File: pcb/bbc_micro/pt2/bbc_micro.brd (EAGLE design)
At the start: 56 x 65 mm, 51 parts, among them IC1 STM32F072C8T6, SW1 324_SW, SW2 324_SW, SW3 324_SW

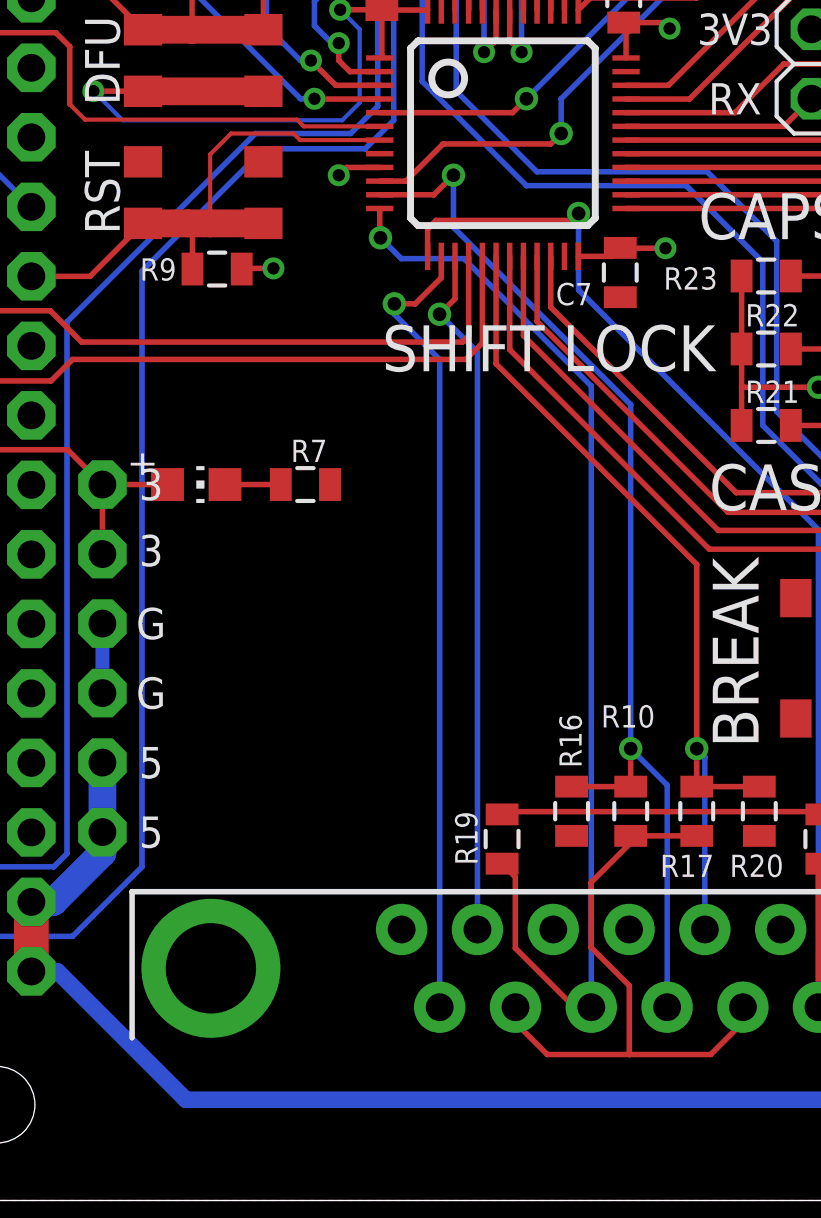
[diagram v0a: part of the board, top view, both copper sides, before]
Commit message: fixed floating VDDA
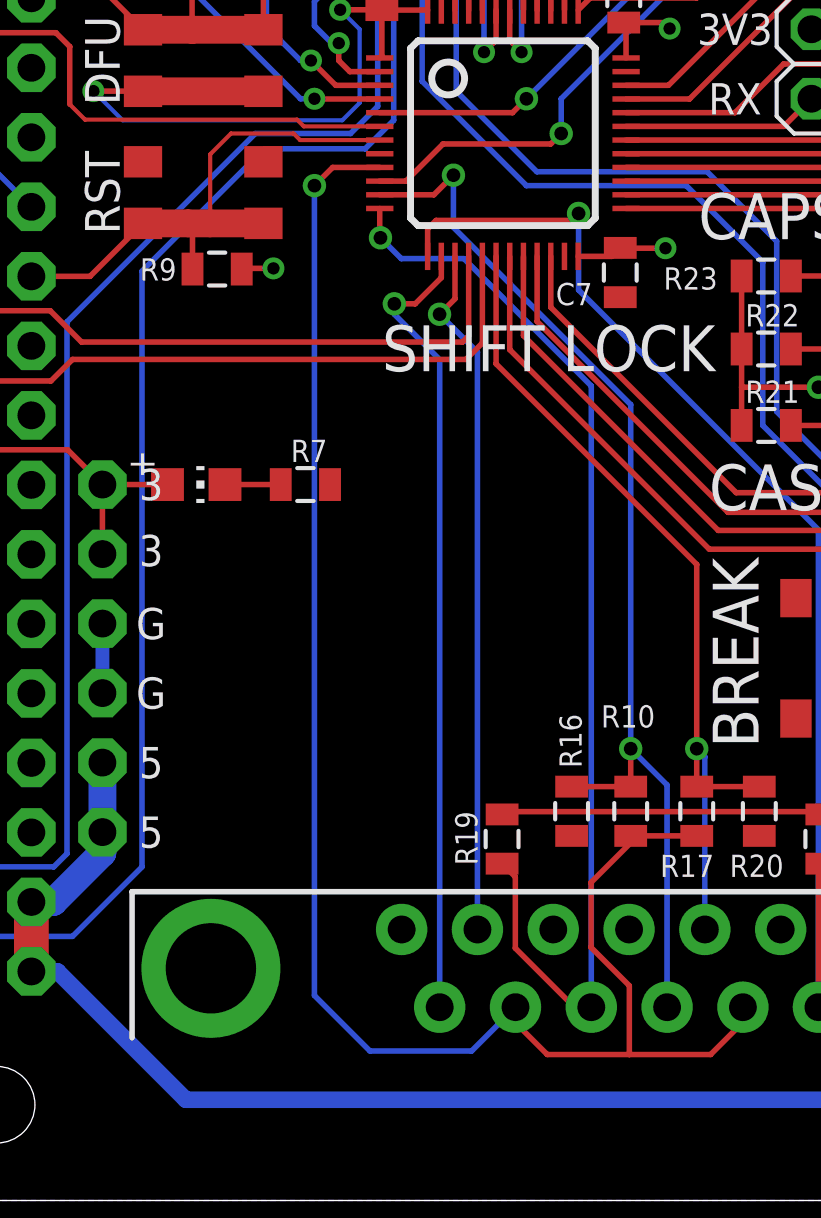
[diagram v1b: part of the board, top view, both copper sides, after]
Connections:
- removed net N$10: R10.1, R17.1, U$9.11, U$9.14
- new net N$11: IC1.9, R10.1, R17.1, U$9.11, U$9.14
- net +3V3: no longer IC1.9
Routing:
- net N$11: track 0.00 -> 63.1 mm, vias 0 -> 1
- net N$10: track 22.0 -> 0.00 mm
- net +3V3: track 45.7 -> 44.1 mm, vias 6 -> 5
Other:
- board text added: "PT0 dekuNukem AUG2022"
- board text removed: "PT3 dekuNukem SEPT2022"
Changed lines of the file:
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@@
 BBC Micro
 </text>
-<text x="24.4348" y="21.1836" size="1.6764" layer="26" rot="MR180" align="center">PT3 dekuNukem SEPT2022</text>
+<text x="24.4348" y="21.1836" size="1.6764" layer="26" rot="MR180" align="center">PT0 dekuNukem AUG2022</text>
 <text x="24.8158" y="17.5006" size="1.9304" layer="26" rot="MR180" align="center">usb4vc.com</text>
 <text x="9.144" y="13.462" size="1.143" layer="25" rot="R180" align="center">5</text>
@@
 <wire x1="16.129" y1="39.4716" x2="8.1026" y2="39.4716" width="0.1524" layer="16"/>
 <wire x1="7.366" y1="26.162" x2="9.745" y2="26.162" width="0.2032" layer="1"/>
-<contactref element="IC1" pad="9"/>
-<via x="16.002" y="37.465" extent="1-16" drill="0.45"/>
-<wire x1="17.5" y1="37.75" x2="16.287" y2="37.75" width="0.2032" layer="1"/>
-<wire x1="16.287" y1="37.75" x2="16.002" y2="37.465" width="0.2032" layer="1"/>
 </signal>
 <signal name="N$29">
@@
 <wire x1="21.07" y1="31" x2="21.07" y2="9.904" width="0.2032" layer="16"/>
 </signal>
+<signal name="N$11">
+<contactref element="R17" pad="1"/>
+<contactref element="R10" pad="1"/>
+<contactref element="U$9" pad="14"/>
+<contactref element="IC1" pad="9"/>
+<contactref element="U$9" pad="11"/>
+<wire x1="30.77" y1="7.064" x2="30.77" y2="6.513" width="0.2032" layer="1"/>
+<wire x1="30.77" y1="6.513" x2="29.591" y2="5.334" width="0.2032" layer="1"/>
+<wire x1="29.591" y1="5.334" x2="26.6192" y2="5.334" width="0.2032" layer="1"/>
+<wire x1="26.6192" y1="5.334" x2="23.622" y2="5.334" width="0.2032" layer="1"/>
+<wire x1="22.46" y1="6.496" x2="22.46" y2="7.064" width="0.2032" layer="1"/>
+<wire x1="23.622" y1="5.334" x2="22.46" y2="6.496" width="0.2032" layer="1"/>
+<wire x1="17.5" y1="37.75" x2="15.779" y2="37.75" width="0.2032" layer="1"/>
+<wire x1="15.779" y1="37.75" x2="15.113" y2="37.084" width="0.2032" layer="1"/>
+<via x="15.113" y="37.084" extent="1-16" drill="0.5"/>
+<wire x1="15.113" y1="37.084" x2="15.113" y2="7.493" width="0.2032" layer="16"/>
+<wire x1="15.113" y1="7.493" x2="17.145" y2="5.461" width="0.2032" layer="16"/>
+<wire x1="17.145" y1="5.461" x2="20.857" y2="5.461" width="0.2032" layer="16"/>
+<wire x1="20.857" y1="5.461" x2="22.46" y2="7.064" width="0.2032" layer="16"/>
+<wire x1="26.67" y1="13.324" x2="29.083" y2="13.324" width="0.2032" layer="1"/>
+<wire x1="26.67" y1="13.324" x2="26.67" y2="13.07" width="0.2032" layer="1"/>
+<wire x1="26.67" y1="13.07" x2="25.2222" y2="11.6222" width="0.2032" layer="1"/>
+<wire x1="26.6192" y1="7.8486" x2="26.6192" y2="5.334" width="0.2032" layer="1"/>
+<wire x1="25.2222" y1="11.6222" x2="25.2222" y2="9.2456" width="0.2032" layer="1"/>
+<wire x1="25.2222" y1="9.2456" x2="26.6192" y2="7.8486" width="0.2032" layer="1"/>
+</signal>
 <signal name="N$17">
 <contactref element="IC1" pad="11"/>
@@
 <wire x1="32.265" y1="39.25" x2="33.274" y2="40.259" width="0.2032" layer="1"/>
 </signal>
-<signal name="N$10">
-<contactref element="R17" pad="1"/>
-<contactref element="R10" pad="1"/>
-<contactref element="U$9" pad="14"/>
-<contactref element="U$9" pad="11"/>
-<wire x1="30.77" y1="7.064" x2="30.77" y2="6.513" width="0.2032" layer="1"/>
-<wire x1="30.77" y1="6.513" x2="29.591" y2="5.334" width="0.2032" layer="1"/>
-<wire x1="29.591" y1="5.334" x2="26.6192" y2="5.334" width="0.2032" layer="1"/>
-<wire x1="26.6192" y1="5.334" x2="23.622" y2="5.334" width="0.2032" layer="1"/>
-<wire x1="22.46" y1="6.496" x2="22.46" y2="7.064" width="0.2032" layer="1"/>
-<wire x1="23.622" y1="5.334" x2="22.46" y2="6.496" width="0.2032" layer="1"/>
-<wire x1="26.67" y1="13.324" x2="29.083" y2="13.324" width="0.2032" layer="1"/>
-<wire x1="26.67" y1="13.324" x2="26.67" y2="13.07" width="0.2032" layer="1"/>
-<wire x1="26.67" y1="13.07" x2="25.2222" y2="11.6222" width="0.2032" layer="1"/>
-<wire x1="26.6192" y1="7.8486" x2="26.6192" y2="5.334" width="0.2032" layer="1"/>
-<wire x1="25.2222" y1="11.6222" x2="25.2222" y2="9.2456" width="0.2032" layer="1"/>
-<wire x1="25.2222" y1="9.2456" x2="26.6192" y2="7.8486" width="0.2032" layer="1"/>
-</signal>
 </signals>
